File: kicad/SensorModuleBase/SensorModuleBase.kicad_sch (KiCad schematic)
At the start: 6 parts, among them J1 Conn_02x08_Top_Bottom, U1 AT28C64B-15PU, U2 74HC00, U3 SN74HC595N, U4 SN74HC595N

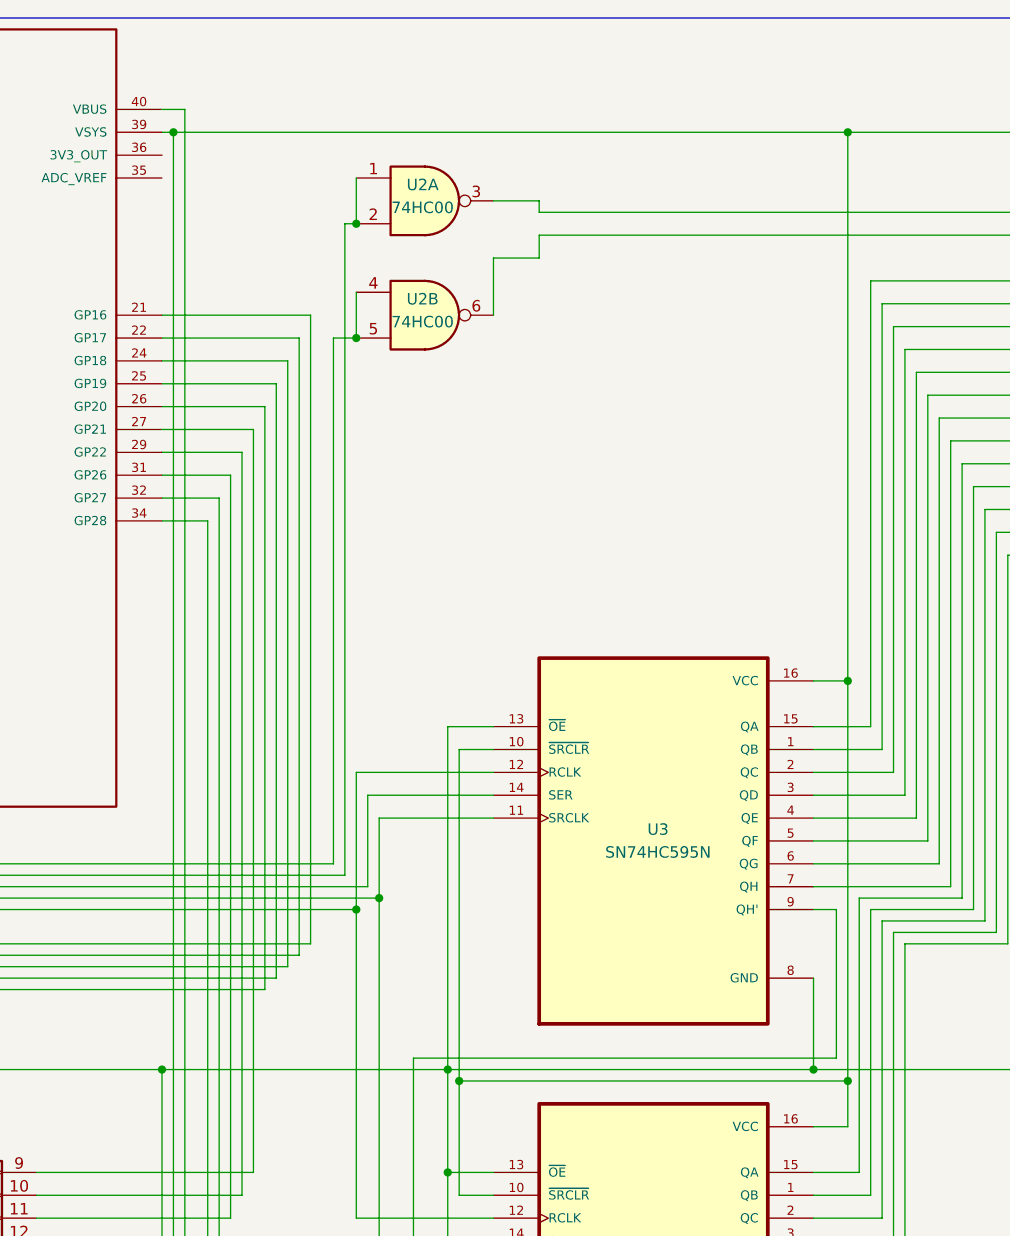
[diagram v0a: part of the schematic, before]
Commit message: added some kicad files and fixed circuit
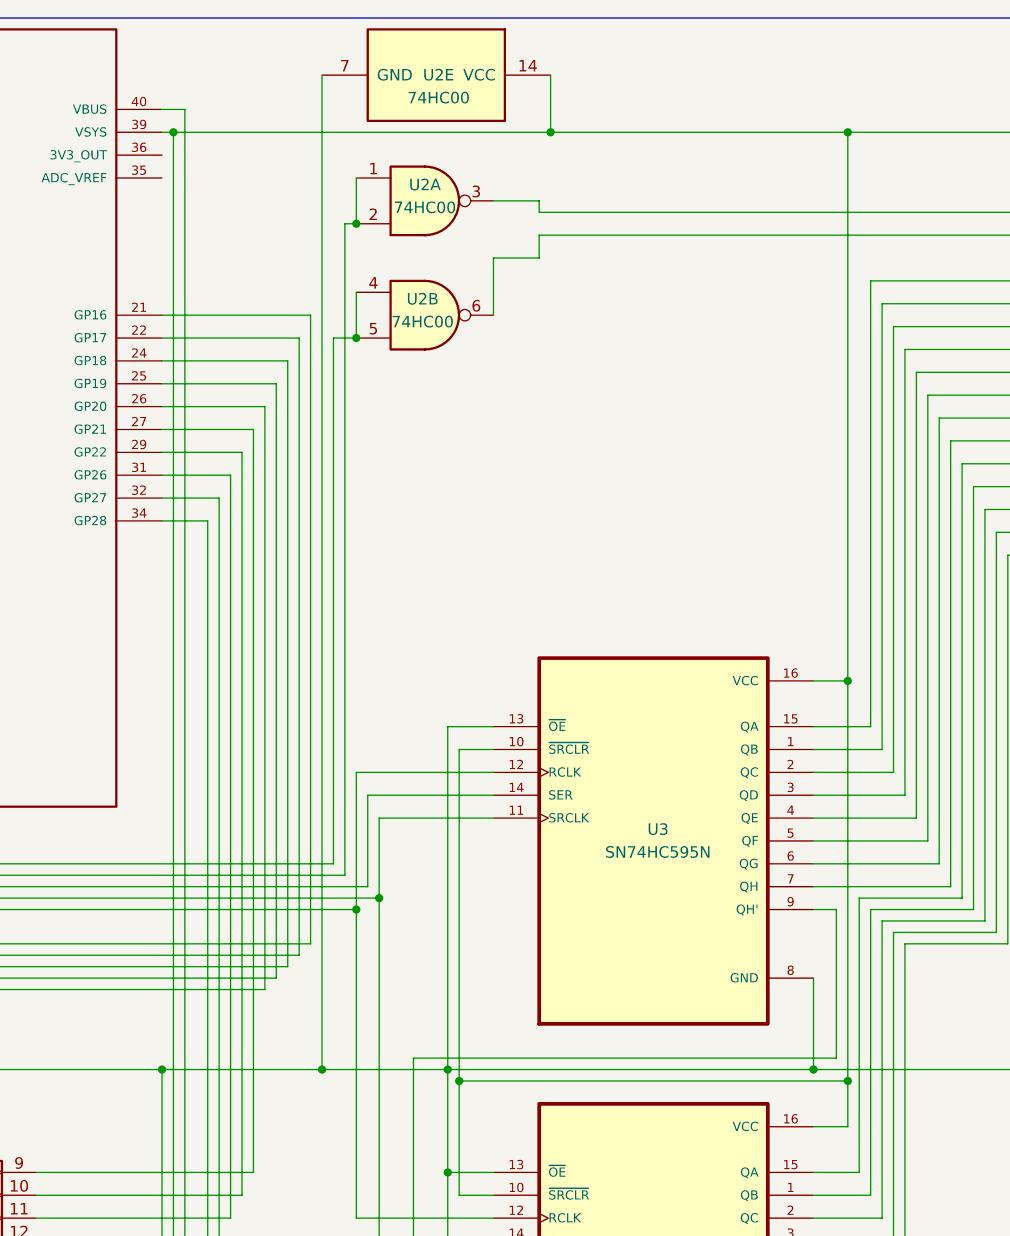
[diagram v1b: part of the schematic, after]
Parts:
- added unit 5 of U2
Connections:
- net at A1.38 (GND), J1.15 (Pin_15), U1.14 (GND)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: now also U2.7 (GND)
- net at A1.39 (VSYS), J1.16 (Pin_16), U1.28 (VCC)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: now also U2.14 (VCC)

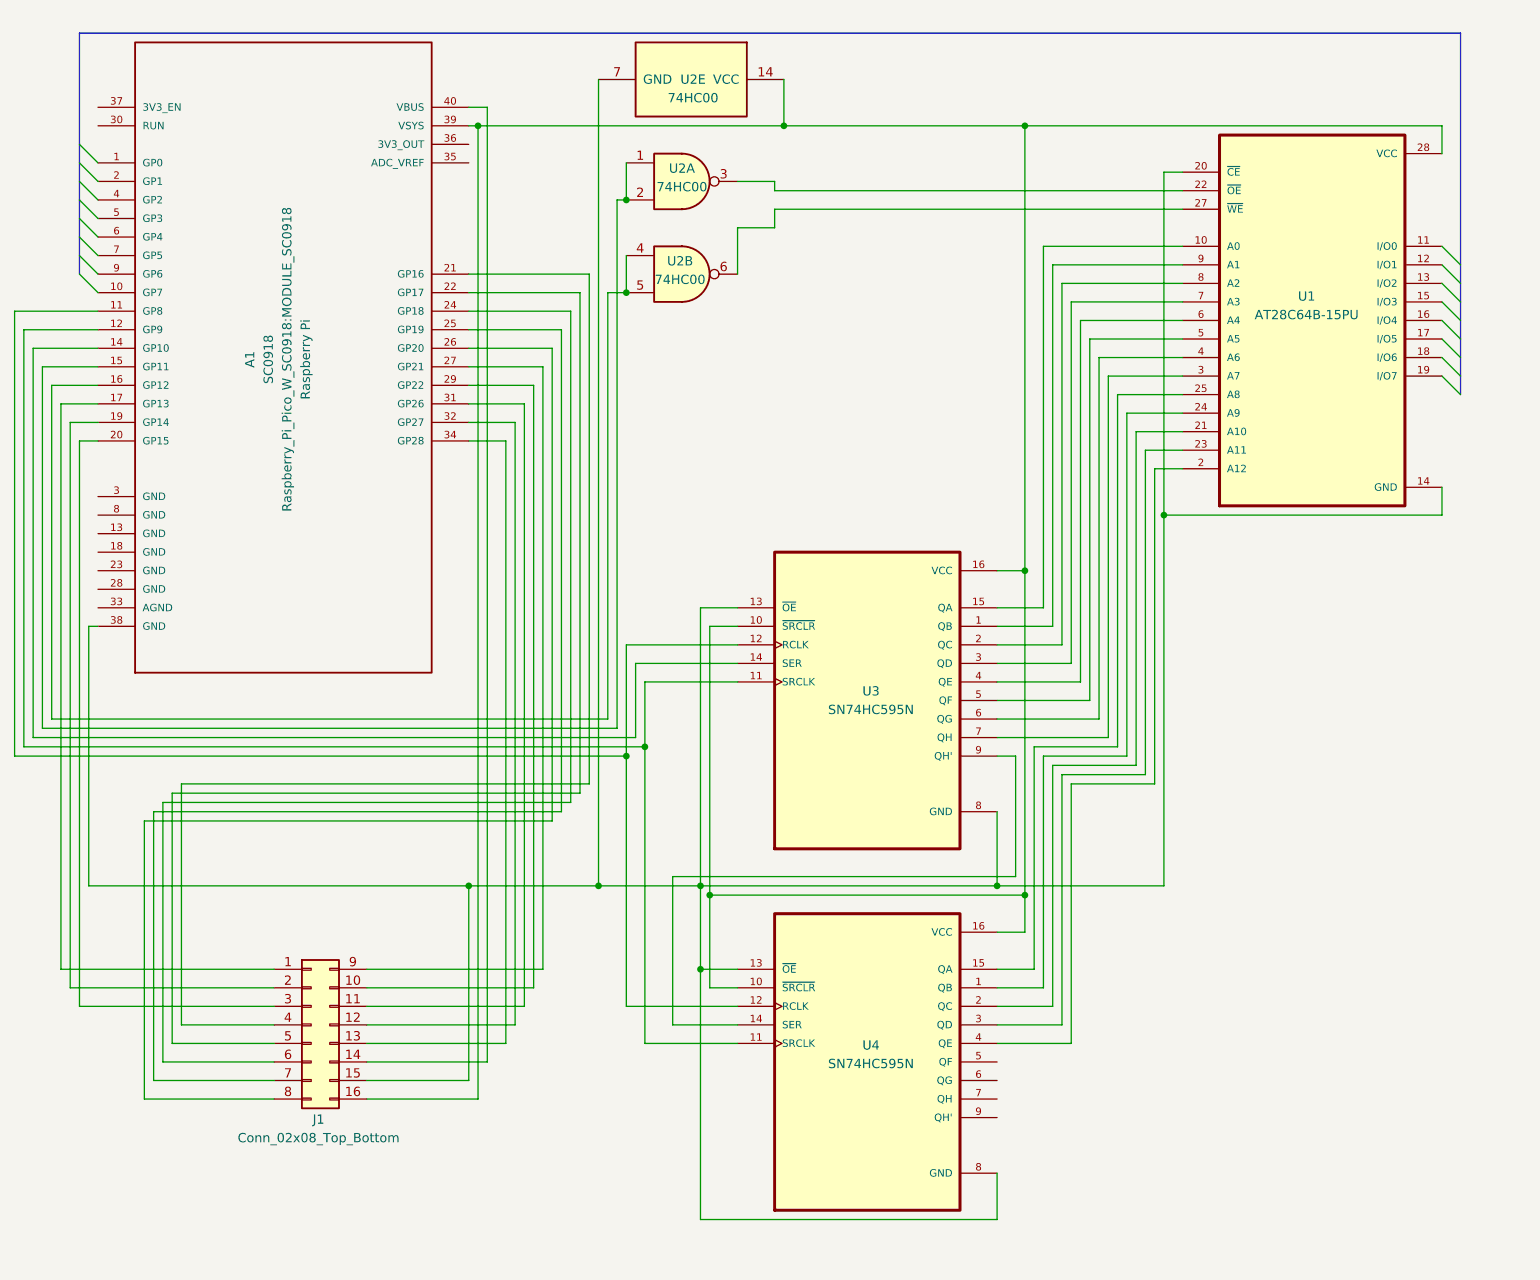
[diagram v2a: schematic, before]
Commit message: Major progress on Serial, KiCAD models, and Python libraries for sensor module base.
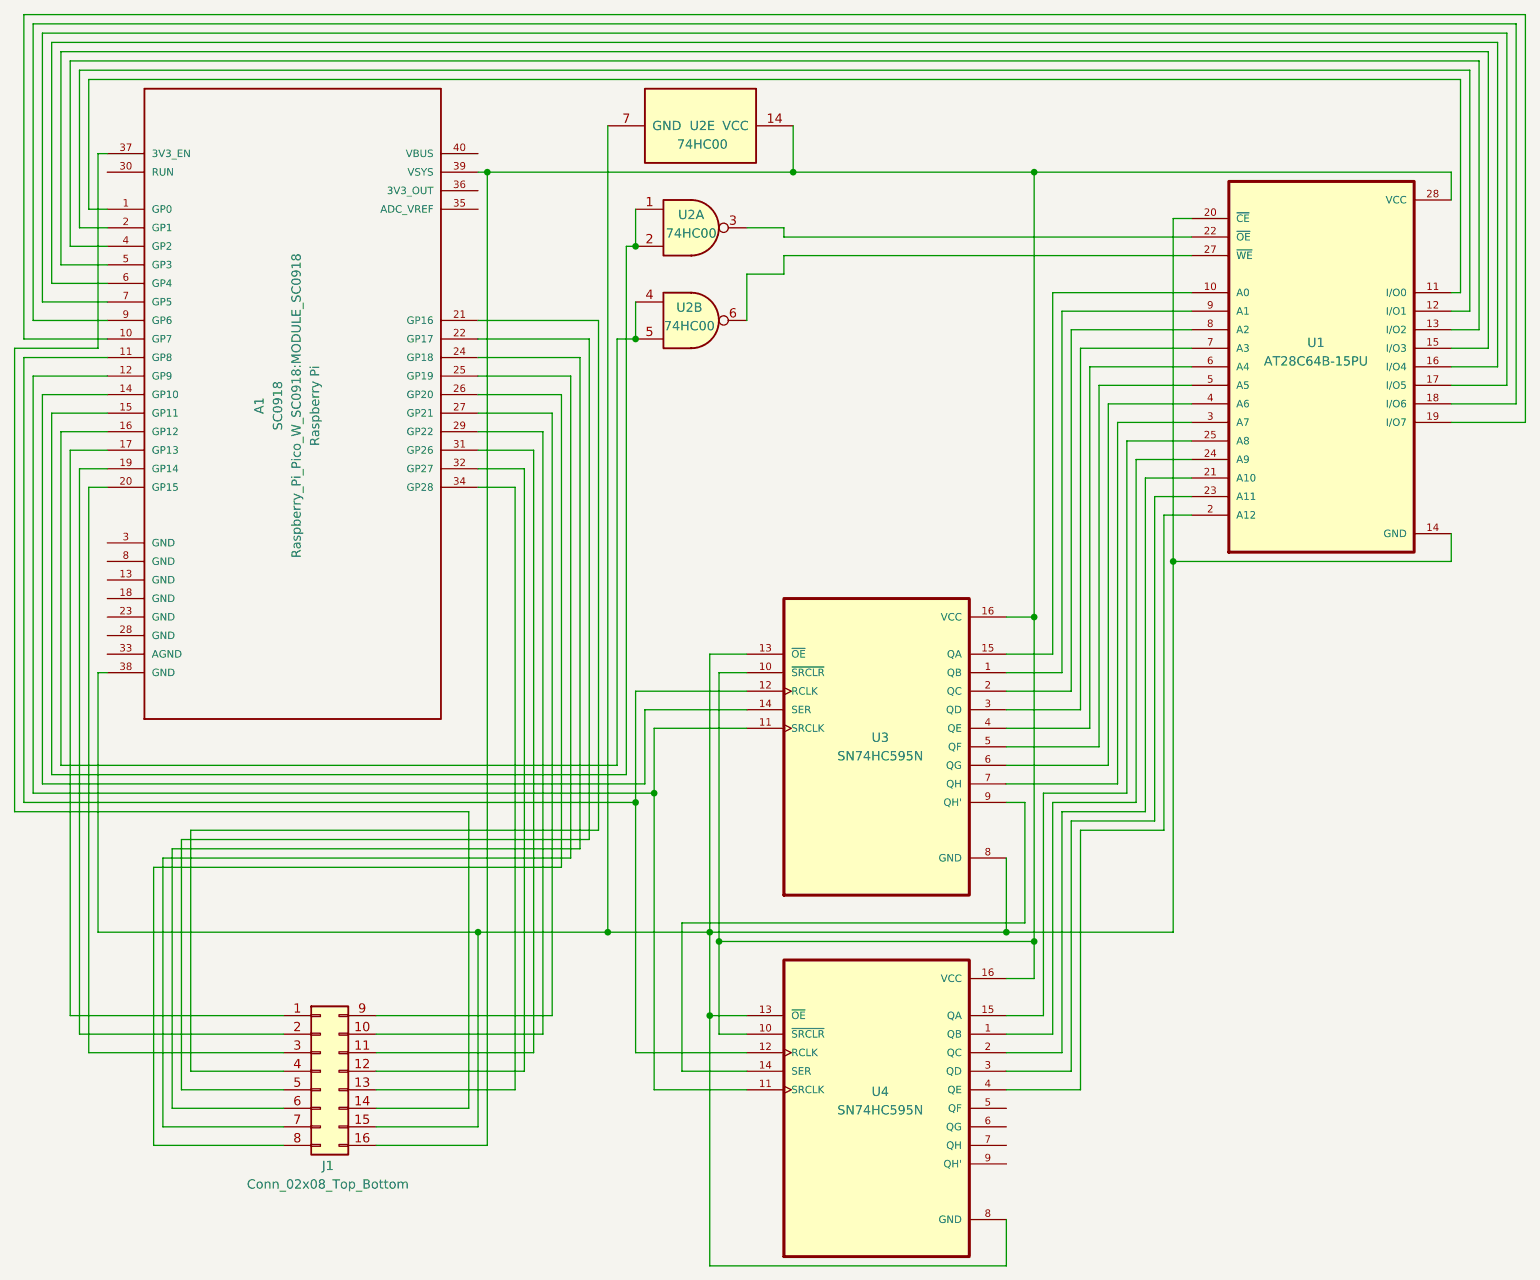
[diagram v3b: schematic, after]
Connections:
- net at J1.14 (Pin_14): now also A1.37 (3V3_EN); no longer A1.40 (VBUS)
- net at U1.11 (I/O0): now also A1.1 (GP0)
- net at U1.12 (I/O1): now also A1.2 (GP1)
- net at U1.13 (I/O2): now also A1.4 (GP2)
- net at U1.15 (I/O3): now also A1.5 (GP3)
- net at U1.16 (I/O4): now also A1.6 (GP4)
- net at U1.17 (I/O5): now also A1.7 (GP5)
- net at U1.18 (I/O6): now also A1.9 (GP6)
- net at U1.19 (I/O7): now also A1.10 (GP7)
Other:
- moved on the sheet: A1, J1, U1, U2A, U2B, U2E, U3, U4
